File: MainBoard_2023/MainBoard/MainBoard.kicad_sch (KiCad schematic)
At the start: 2 parts

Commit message: 電源設計終了
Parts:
- added C?: 1μ, symbol Device:C_Small
- added C?: 10μ, symbol Device:C_Small
- added IC?: IP2721D, SOP65P640X120-16N, symbol IP2721:IP2721D
- added J?: UJC-HP-3-SMT-TR, CUI_UJC-HP-3-SMT-TR, symbol USB_TypeC_6PIN:UJC-HP-3-SMT-TR
- added Q?: AO3400A, SOT95P280X125-3N, symbol AO3400A:AO3400A
- added R? (x2): 5.1k, symbol Device:R_Small
- added U?: Adafruit_BNO055_STEMMA_QT, symbol Adafruit_BNO055_STEMMA_QT:Adafruit_BNO055_STEMMA_QT
- added U?: SC0915, MODULE_SC0915, symbol Raspberry_Pi_Pico:SC0915
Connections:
- new net: IC?.1 (VBUSG), Q?.1
- new net: U?.13 (GND), U?.18 (GND), U?.23 (GND), U?.28 (GND), U?.3 (GND), U?.38 (GND), U?.8 (GND), U?.D2 (GND)
- new net +12VA: C?.1, IC?.16 (VBUS), Q?.2
- new net CC1: IC?.13 (CC1), J?.A5 (CC1), R?.1
- new net CC2: IC?.12 (CC2), J?.B5 (CC2), R?.1
- new net GNDA: C?.2, C?.2, IC?.5 (GND), J?.A12 (GND), J?.B12 (GND), J?.S1 (SHIELD), J?.S2 (SHIELD), J?.S3 (SHIELD), J?.S4 (SHIELD), R?.2, R?.2
- new net SELP: IC?.6 (SELP)
- new net VBUS: C?.1, IC?.11 (SEL), IC?.2 (VIN), J?.A9 (V-BUS), J?.B9 (V-BUS), Q?.3
- no-connect marks 0 -> 8
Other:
- added sheet AudioAmplifier (AudioAmplifier.kicad_sch)
- note added: "High 12V Float 9V GND 5V"
- note added: "USB PD"
- moved on the sheet: U?

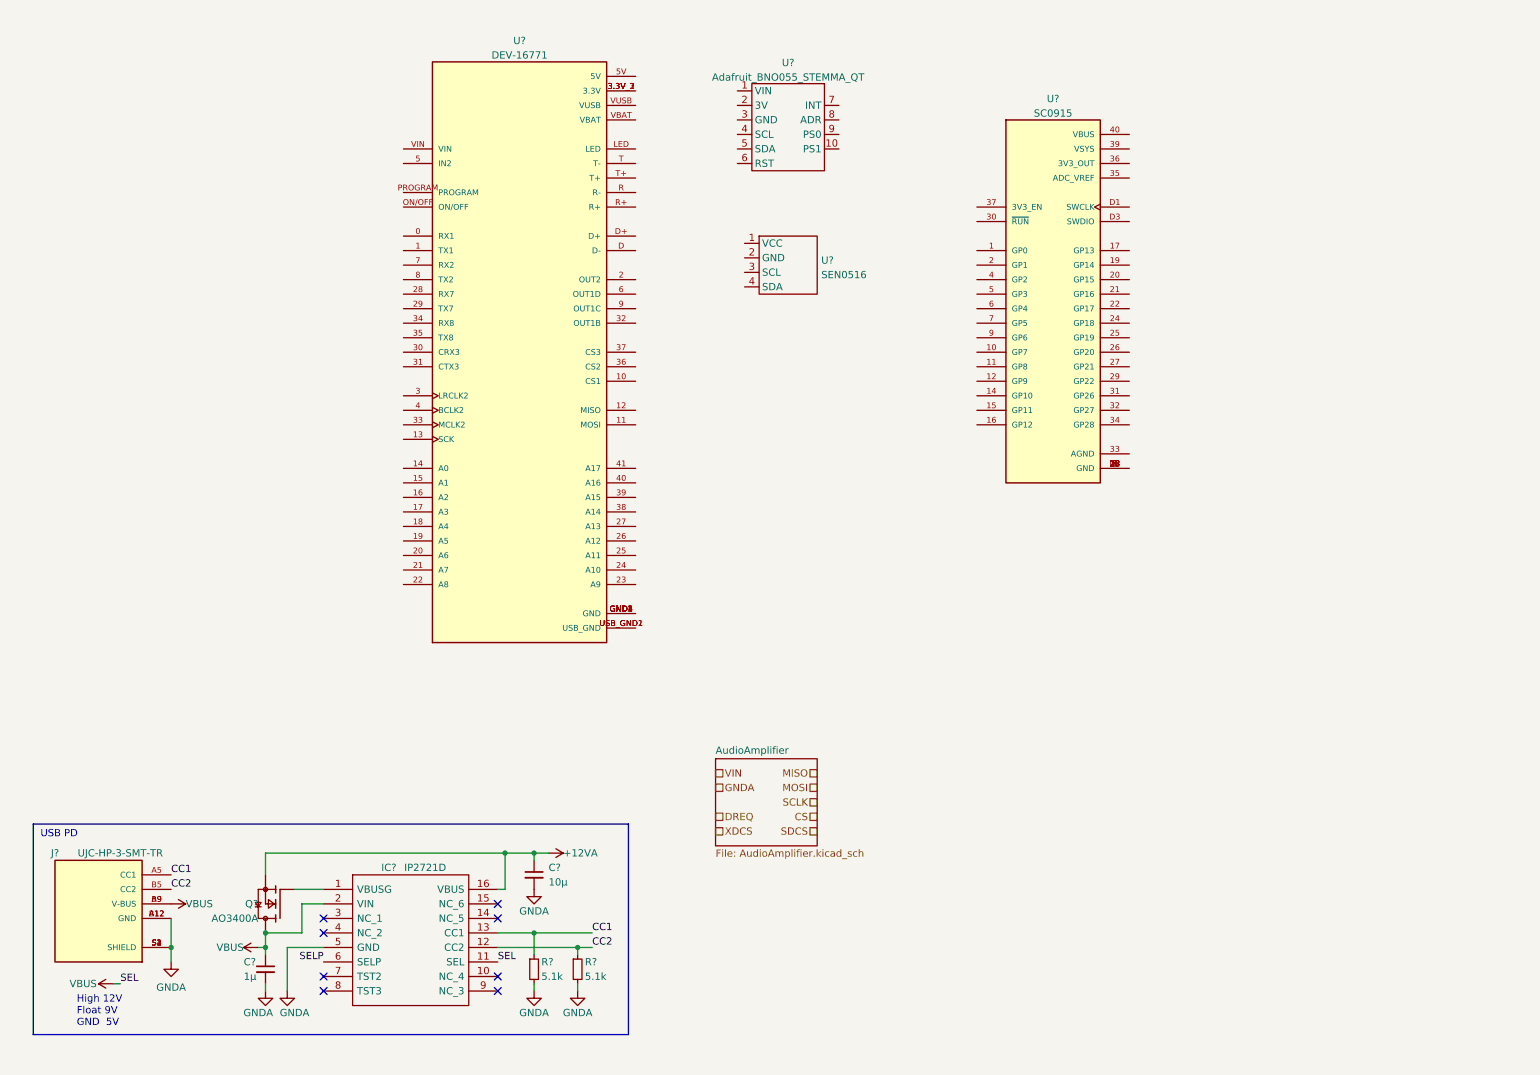
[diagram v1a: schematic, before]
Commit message: レギュレータを配置
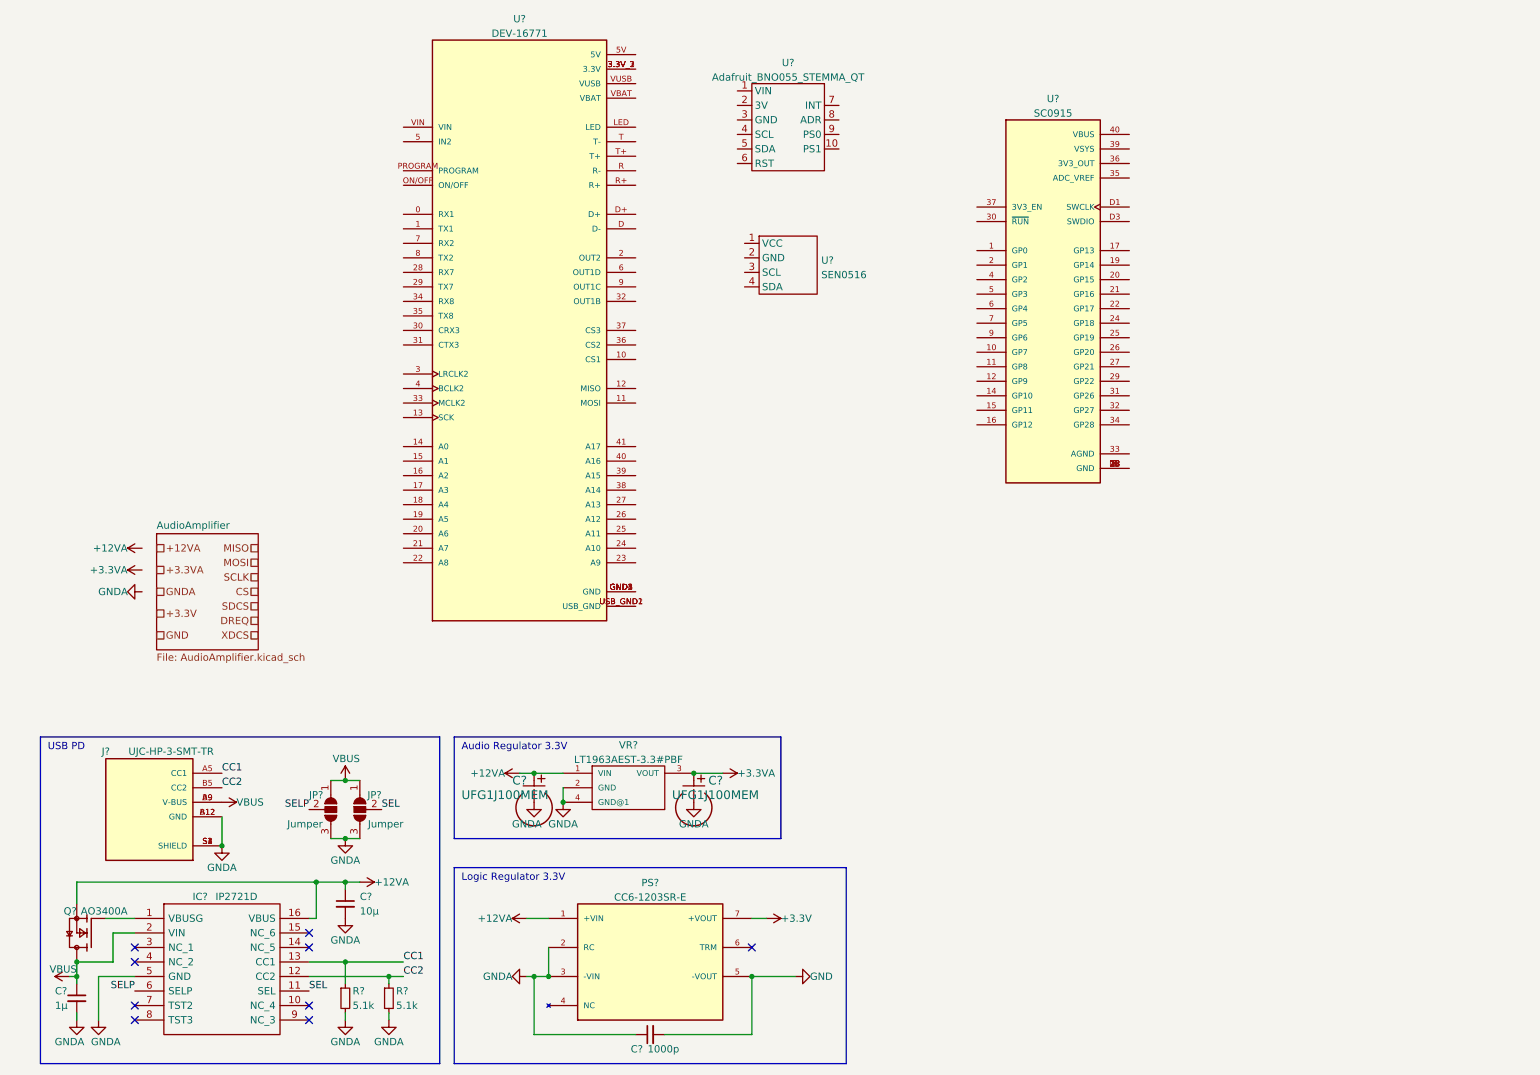
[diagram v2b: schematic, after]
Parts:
- added C?: 1000p, Capacitor_SMD:C_0603_1608Metric_Pad1.08x0.95mm_HandSolder, symbol Device:C_Small
- added C? (x2): UFG1J100MEM, PCAP_6_3x11THRU-ELECT_NCA, symbol UFG1J100MEM:UFG1J100MEM
- added JP? (x2): Jumper, symbol Jumper:SolderJumper_3_Open
- added PS?: CC6-1203SR-E, CONV_CC6-1203SR-E, symbol CC6-1203SR-E:CC6-1203SR-E
- added VR?: LT1963AEST-3.3#PBF, SOT223, symbol LT1963AEST-3.3_PBF:LT1963AEST-3.3#PBF
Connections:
- net +12VA: now also C?.1, PS?.1 (+VIN), VR?.1 (VIN)
- net GNDA: now also C?.1, C?.2, C?.2, JP?.3 (B), JP?.3 (B), PS?.2 (RC), PS?.3 (-VIN), VR?.2 (GND), VR?.4 (GND@1)
- net SELP: now also JP?.2 (C)
- net VBUS: now also JP?.1 (A), JP?.1 (A); no longer IC?.11 (SEL)
- new net +3.3V: PS?.7 (+VOUT)
- new net +3.3VA: C?.1, VR?.3 (VOUT)
- new net GND: C?.2, PS?.5 (-VOUT)
- new net SEL: IC?.11 (SEL), JP?.2 (C)
- no-connect marks 8 -> 9
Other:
- note added: "Audio Regulator 3.3V"
- note added: "Logic Regulator 3.3V"
- note removed: "High 12V Float 9V GND 5V"
- moved on the sheet: C?, IC?, J?, Q?, R?, U?

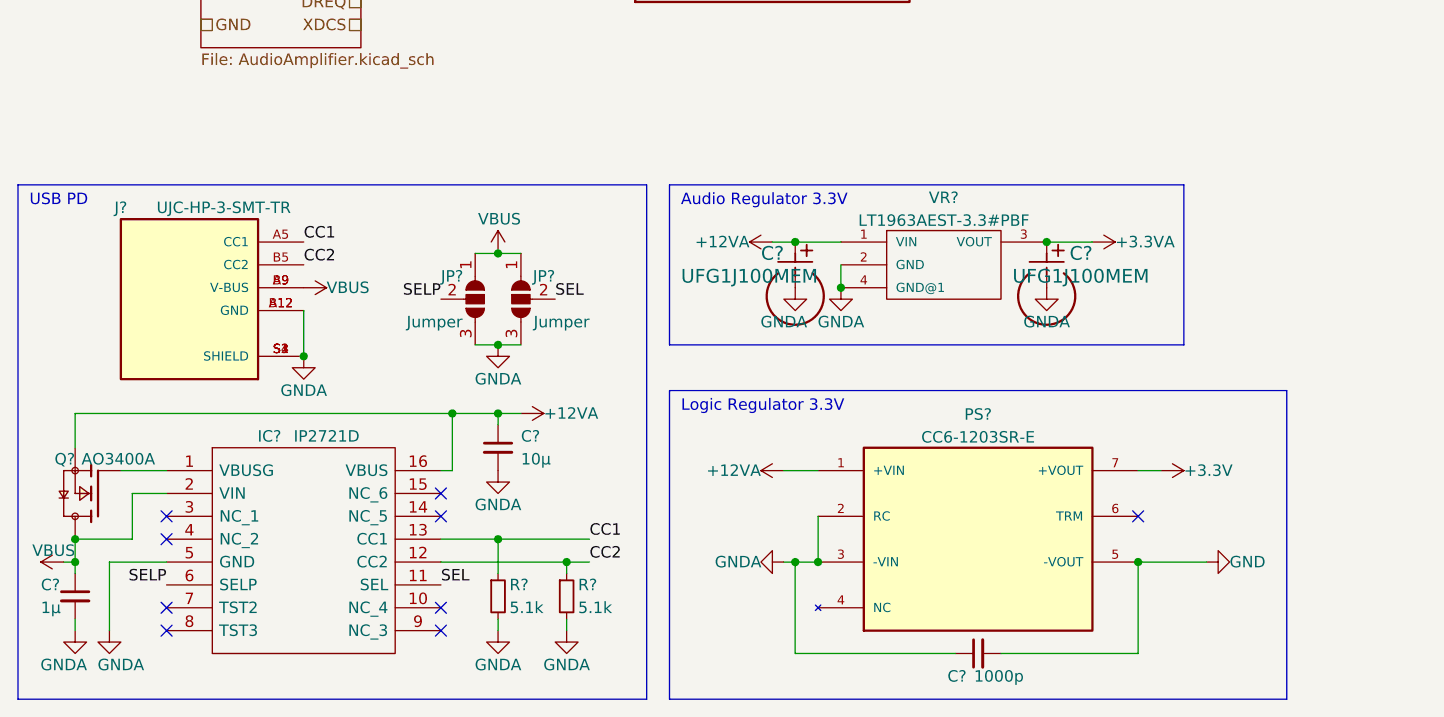
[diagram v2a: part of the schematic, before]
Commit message: EMIフィルタをライブラリに追加
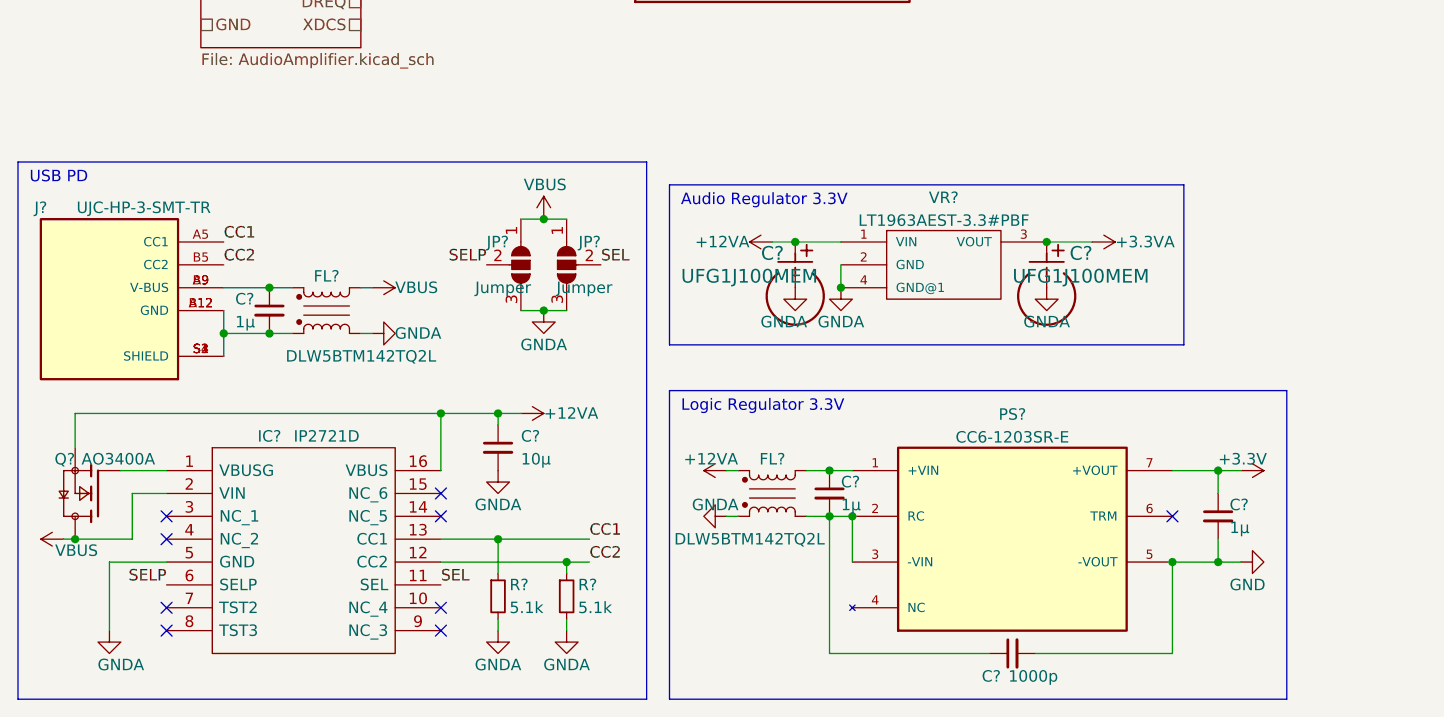
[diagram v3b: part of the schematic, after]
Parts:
- removed C?: 1μ, symbol Device:C_Small
- added C? (x3): 1μ, symbol Device:C_Small
- added FL? (x2): DLW5BTM142TQ2L, FIL_DLW5BTM142TQ2L, symbol DLW5BTM142TQ2:DLW5BTM142TQ2L
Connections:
- net +12VA: now also FL?.1; no longer PS?.1 (+VIN)
- net +3.3V: now also C?.1
- net GND: now also C?.2
- net GNDA: now also FL?.3, FL?.4; no longer C?.1, J?.A12 (GND), J?.B12 (GND), J?.S1 (SHIELD), J?.S2 (SHIELD), J?.S3 (SHIELD), J?.S4 (SHIELD), PS?.2 (RC), PS?.3 (-VIN)
- net VBUS: now also FL?.2; no longer J?.A9 (V-BUS), J?.B9 (V-BUS)
- new net: C?.1, FL?.1, J?.A9 (V-BUS), J?.B9 (V-BUS)
- new net: C?.2, FL?.4, J?.A12 (GND), J?.B12 (GND), J?.S1 (SHIELD), J?.S2 (SHIELD), J?.S3 (SHIELD), J?.S4 (SHIELD)
- new net: C?.1, FL?.2, PS?.1 (+VIN)
- new net: C?.1, C?.2, FL?.3, PS?.2 (RC), PS?.3 (-VIN)
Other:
- moved on the sheet: C?, J?, JP?, PS?

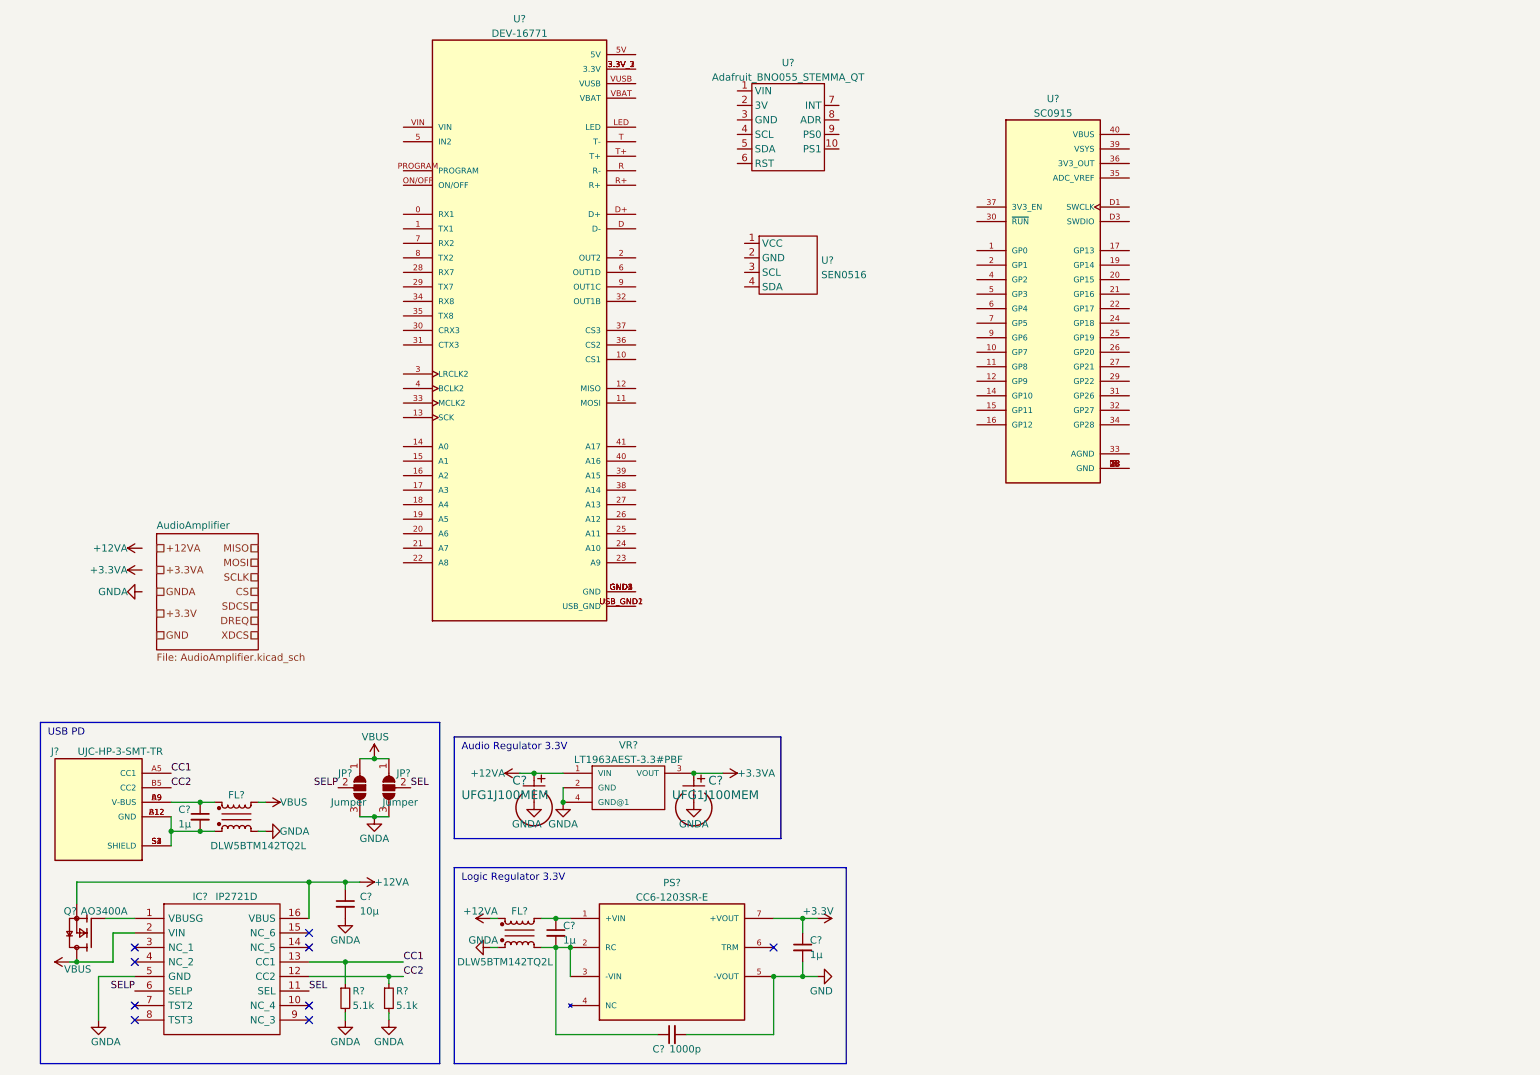
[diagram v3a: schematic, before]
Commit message: 電源回路を修正
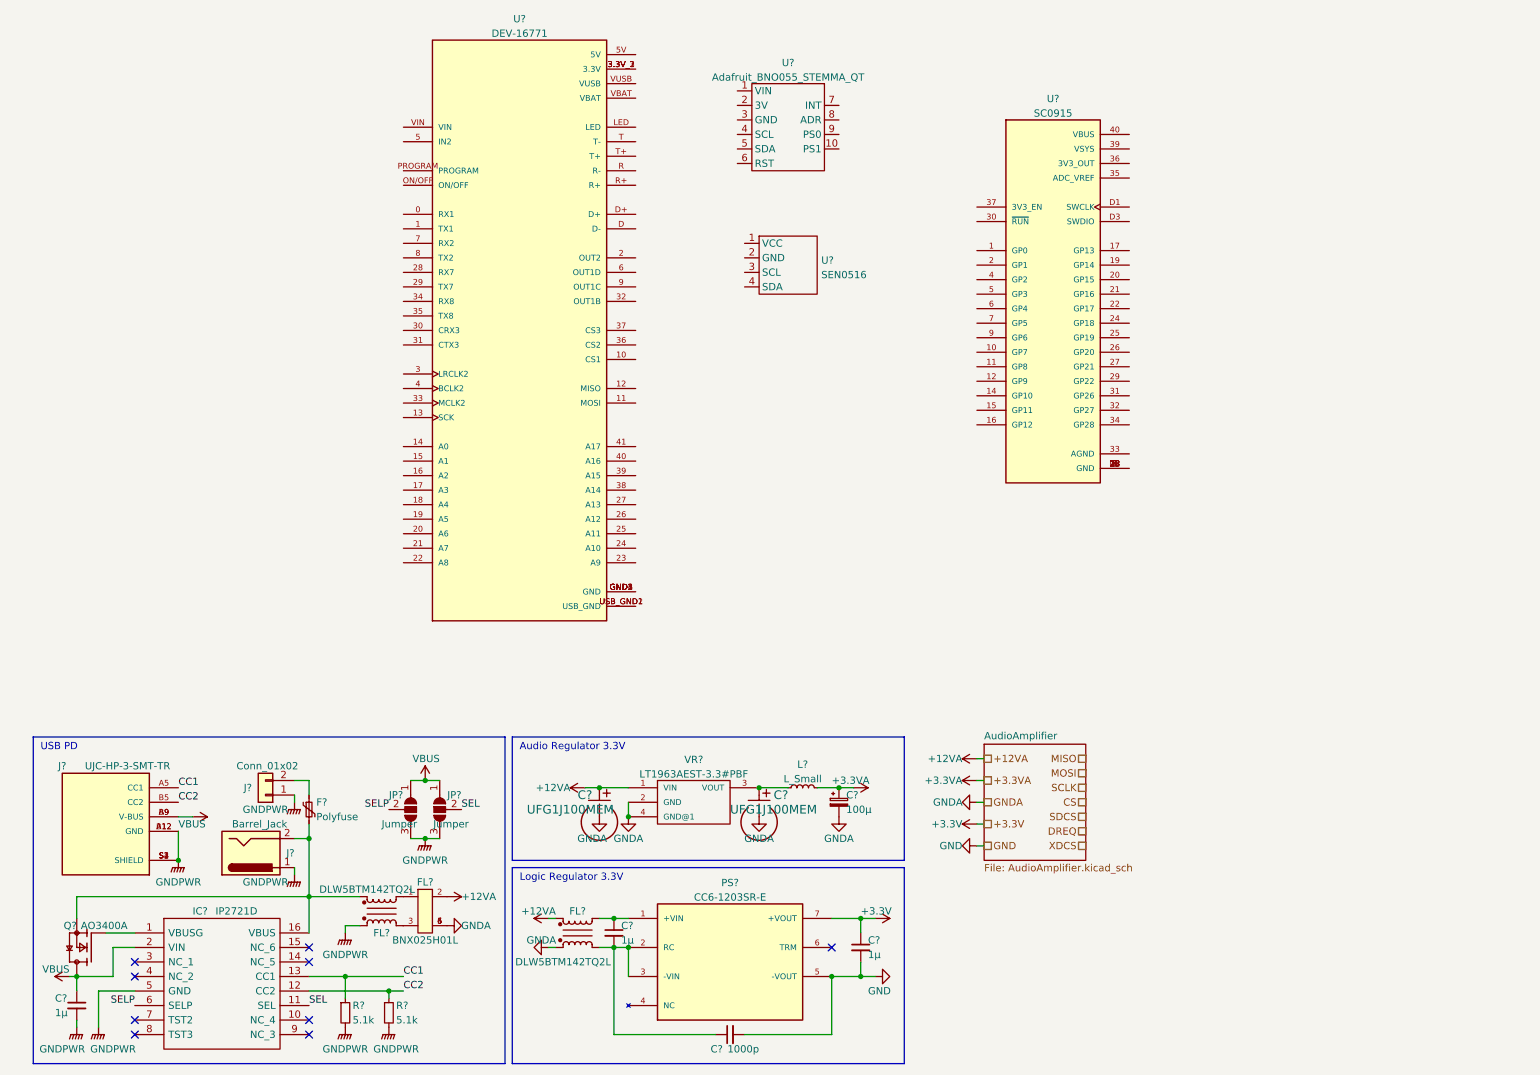
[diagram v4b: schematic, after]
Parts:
- removed C?: 1μ, symbol Device:C_Small
- removed C?: 10μ, symbol Device:C_Small
- removed FL?: DLW5BTM142TQ2L, FIL_DLW5BTM142TQ2L, symbol DLW5BTM142TQ2:DLW5BTM142TQ2L
- added C?: 100μ, symbol Device:C_Polarized_Small
- added C?: 1μ, symbol Device:C_Small
- added F?: Polyfuse, symbol Device:Polyfuse_Small
- added FL?: DLW5BTM142TQ2L, FIL_DLW5BTM142TQ2L, symbol DLW5BTM142TQ2:DLW5BTM142TQ2L
- added FL?: BNX025H01L, FIL_BNX025H01L, symbol BNX025H01:BNX025H01L
- added J?: Conn_01x02, symbol Connector_Generic:Conn_01x02
- added J?: Barrel_Jack, symbol Connector:Barrel_Jack
- added L?: L_Small, symbol Device:L_Small
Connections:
- net +12VA: now also FL?.2; no longer IC?.16 (VBUS), Q?.2
- net +3.3VA: now also C?.1, L?.2; no longer C?.1, VR?.3 (VOUT)
- net GNDA: now also C?.2, FL?.4, FL?.5, FL?.6; no longer IC?.5 (GND), JP?.3 (B), JP?.3 (B), R?.2, R?.2
- net VBUS: now also J?.A9 (V-BUS), J?.B9 (V-BUS), C?.1
- net GNDPWR: now reaches J?.A12 (GND), J?.B12 (GND), J?.S1 (SHIELD), J?.S2 (SHIELD), J?.S3 (SHIELD), J?.S4 (SHIELD)
- net GNDPWR: now also IC?.5 (GND), JP?.3 (B), JP?.3 (B), R?.2, R?.2, C?.2, FL?.4, J?.1, J?.1 (Pin_1)
- new net: F?.1, J?.2 (Pin_2)
- new net: F?.2, FL?.1, IC?.16 (VBUS), J?.2, Q?.2
- new net: C?.1, L?.1, VR?.3 (VOUT)
- new net: FL?.1, FL?.2
- new net: FL?.3, FL?.3
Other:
- moved on the sheet: C?, FL?, IC?, J?, JP?, PS?, Q?, R?, VR?
